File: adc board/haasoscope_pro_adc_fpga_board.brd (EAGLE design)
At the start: 224.5 x 160 mm, 569 parts, among them CN2 12Vin, IC1 ADC12DL2500ACF, IC10 TPS72325DBVR, IC13 LMH5401IRMST, IC14 LMH6401IRMZR, IC15 SN74AVC4T774PWR, IC17 DAC8562SDGSR, IC18 TLV9102IPWR, IC2 SN74AVC4T774PWR, IC21 LMH5401IRMST, IC22 TPS7A7200RGTR, IC23 TPS7A7200RGTR, IC24 TPS7A7200RGTR, IC25 TPS72325DBVR, IC26 TPS7A7200RGTR, IC27 TPS7A7200RGTR, IC28 TPS7A7200RGTR, IC29 LMH6401IRMZR, IC3 ADC122S021CIMM_NOPB, IC30 SN74AVC4T774PWR, IC33 TLV9102IPWR, IC4 TLV9102IPWR, IC5 EP4CE30F23C6N, IC6 EPCQ16ASI8N, IC7 TPS7A7200RGTR, IC8 FT232HQ, IC9 93LC56B, J1 2p-2.54, J10 8pin, J11 8pin, J13 8pin, J14 2x5, J15 test1, J2 test1, J3 2p-2.54, J30 2p-2.54, J31 2p-2.54, J32 2p-2.54, J33 2p-2.54, J34 2p-2.54, J35 2p-2.54, J36 2p-2.54, J37 2p-2.54, J39 2p-2.54, J4 2p-2.54, J40 2p-2.54, J41 2p-2.54, J42 2p-2.54, J43 2p-2.54, J44 2p-2.54, J45 2p-2.54, J46 2p-2.54, J8 8pin, K1 G6K-2F-RF-T-TR03_DC5, K2 G6K-2F-RF-T-TR03_DC5, K3 G6K-2F-RF-T-TR03_DC5, K4 G6K-2F-RF-T-TR03_DC5, K5 G6K-2F-RF-T-TR03_DC5, K6 TLP3475R_TP,F, K7 TLP3475R_TP,F, Q1 S8050, Q4 S8050, Q5 S8050, Q7 S8050, Q8 S8050, Q9 S8050, SW3 SKQGADE010, SW4 SKQGADE010, U2 ADF4350BCPZ, X1 USBC, Y2 OSCILLATORSMD-5X3, Y3 12MHz

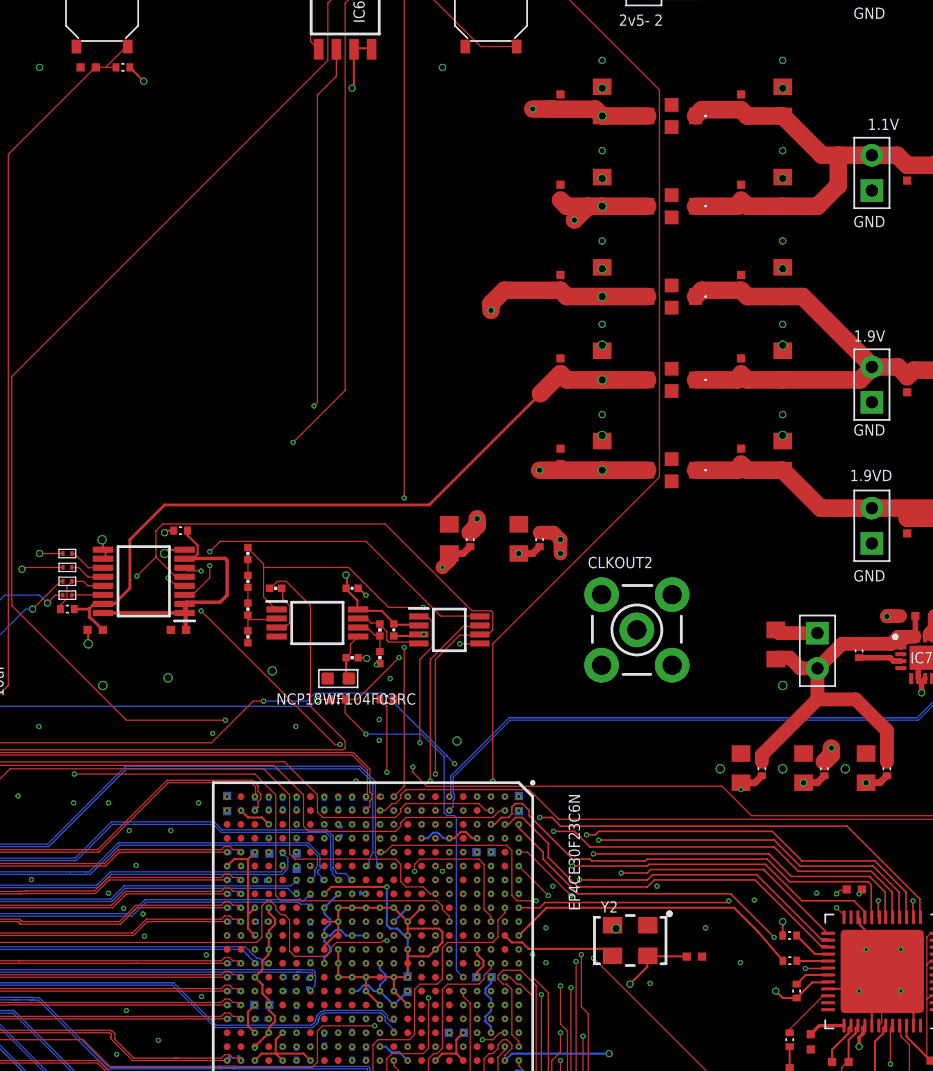
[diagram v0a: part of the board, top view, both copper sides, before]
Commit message: use 0.35mm vias instead of a few 0.5mm ones
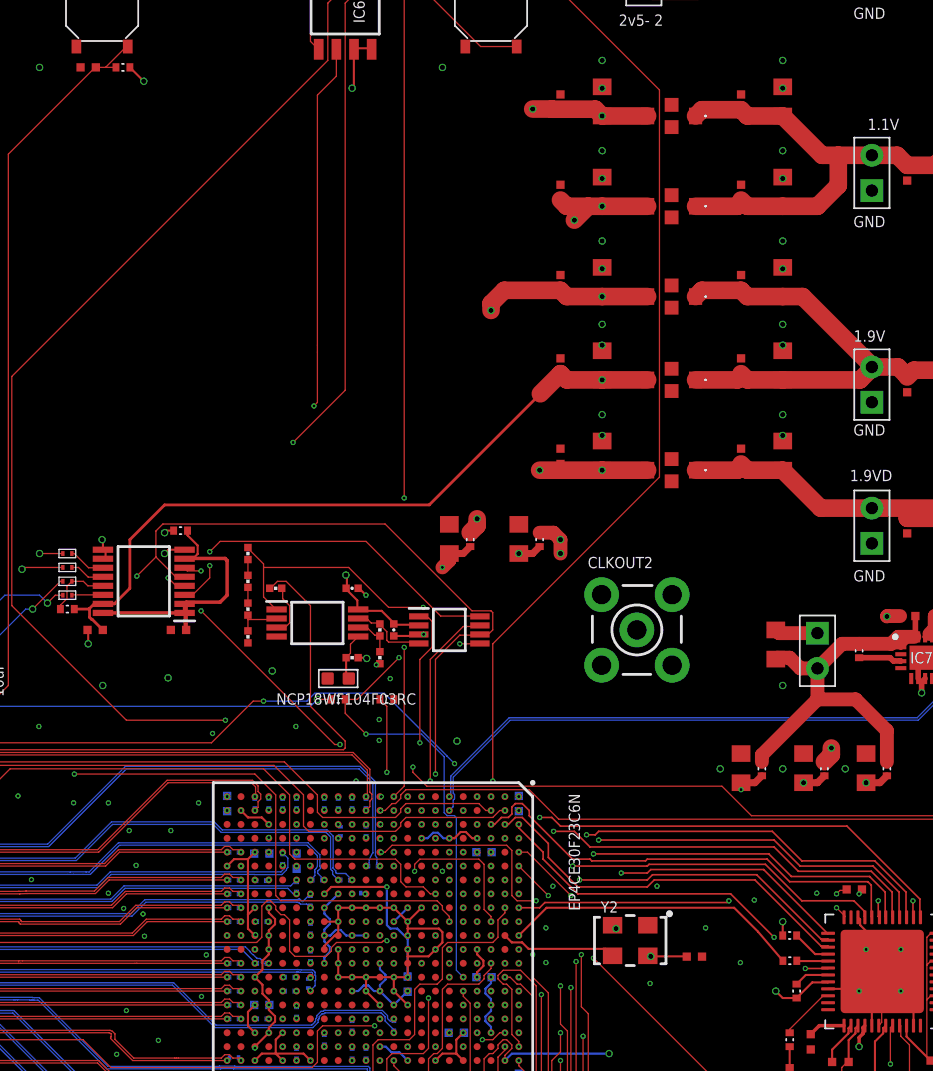
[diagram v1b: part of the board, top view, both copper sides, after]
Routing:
- net 3V3: track 157.8 -> 155.5 mm
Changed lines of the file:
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@@
 <wire x1="101.5" y1="68.65" x2="101.5" y2="69" width="0.1524" layer="16"/>
 <via x="103.5" y="82" extent="1-16" drill="0.2"/>
-<via x="129.5" y="80.5" extent="1-16" drill="0.5"/>
+<via x="129.5" y="80.5" extent="1-16" drill="0.35"/>
 <via x="69.5" y="68.5" extent="1-16" drill="0.2"/>
 <via x="73" y="69" extent="1-16" drill="0.2"/>
@@
 <via x="61.5" y="81" extent="1-16" drill="0.2"/>
 <via x="62" y="78" extent="1-16" drill="0.2"/>
-<via x="128.5" y="134.5" extent="1-16" drill="0.5"/>
-<via x="141.5" y="134.5" extent="1-16" drill="0.5"/>
-<via x="141.5" y="141" extent="1-16" drill="0.5"/>
-<via x="141.5" y="128" extent="1-16" drill="0.5"/>
-<via x="128.5" y="128" extent="1-16" drill="0.5"/>
-<via x="128.5" y="141" extent="1-16" drill="0.5"/>
-<via x="128.5" y="122.5" extent="1-16" drill="0.5"/>
-<via x="141.5" y="122.5" extent="1-16" drill="0.5"/>
-<via x="141.5" y="116" extent="1-16" drill="0.5"/>
-<via x="128.5" y="116" extent="1-16" drill="0.5"/>
-<via x="91.5" y="101" extent="1-16" drill="0.5"/>
+<via x="128.5" y="134.5" extent="1-16" drill="0.35"/>
+<via x="141.5" y="134.5" extent="1-16" drill="0.35"/>
+<via x="141.5" y="141" extent="1-16" drill="0.35"/>
+<via x="141.5" y="128" extent="1-16" drill="0.35"/>
+<via x="128.5" y="128" extent="1-16" drill="0.35"/>
+<via x="128.5" y="141" extent="1-16" drill="0.35"/>
+<via x="128.5" y="122.5" extent="1-16" drill="0.35"/>
+<via x="141.5" y="122.5" extent="1-16" drill="0.35"/>
+<via x="141.5" y="116" extent="1-16" drill="0.35"/>
+<via x="128.5" y="116" extent="1-16" drill="0.35"/>
+<via x="91.5" y="101" extent="1-16" drill="0.35"/>
 <via x="103.5" y="79" extent="1-16" drill="0.2"/>
 <via x="116.5" y="71" extent="1-16" drill="0.2"/>
@@
 <via x="53" y="94" extent="1-16" drill="0.35"/>
 <via x="68" y="97.5" extent="1-16" drill="0.35"/>
-<via x="92.55" y="98" extent="1-16" drill="0.5"/>
-<via x="104.75" y="99.05" extent="1-16" drill="0.5"/>
-<via x="118.05" y="94" extent="1-16" drill="0.5"/>
+<via x="92.55" y="98" extent="1-16" drill="0.35"/>
+<via x="104.75" y="99.05" extent="1-16" drill="0.35"/>
+<via x="118.05" y="94" extent="1-16" drill="0.35"/>
 <via x="72.55" y="94" extent="1-16" drill="0.2"/>
 <via x="69" y="90.5" extent="1-16" drill="0.2"/>
@@
 <via x="81.5" y="87" extent="1-16" drill="0.2"/>
 <via x="82.5" y="87" extent="1-16" drill="0.2"/>
-<via x="141.5" y="98" extent="1-16" drill="0.5"/>
+<via x="141.5" y="98" extent="1-16" drill="0.35"/>
 <wire x1="161.7" y1="101.2" x2="162.8521" y2="101.2" width="0.25" layer="1"/>
 <wire x1="162.8521" y1="101.2" x2="162.921" y2="101.1311" width="0.25" layer="1"/>
@@
 <via x="58.5" y="89" extent="1-16" drill="0.35"/>
 <via x="58.5" y="93" extent="1-16" drill="0.35"/>
-<via x="97" y="107.5" extent="1-16" drill="0.5"/>
+<via x="97" y="107.5" extent="1-16" drill="0.35"/>
 <wire x1="97" y1="107.5" x2="97.275" y2="107.775" width="0.1524" layer="1"/>
 <wire x1="97.275" y1="107.775" x2="98.438" y2="107.775" width="0.1524" layer="1"/>
-<via x="92.5" y="108.5" extent="1-16" drill="0.5"/>
+<via x="92.5" y="108.5" extent="1-16" drill="0.35"/>
 <wire x1="92.5" y1="108.5" x2="92.562" y2="108.438" width="0.1524" layer="1"/>
 <wire x1="92.562" y1="108.438" x2="92.562" y2="107.775" width="0.1524" layer="1"/>
@@
 <via x="141.5" y="136.5" extent="1-16" drill="0.35"/>
 <via x="141.5" y="143" extent="1-16" drill="0.35"/>
-<via x="137" y="92" extent="1-16" drill="0.5"/>
-<via x="141.5" y="92" extent="1-16" drill="0.5"/>
-<via x="146" y="92" extent="1-16" drill="0.5"/>
+<via x="137" y="92" extent="1-16" drill="0.35"/>
+<via x="141.5" y="92" extent="1-16" drill="0.35"/>
+<via x="146" y="92" extent="1-16" drill="0.35"/>
 <via x="152.930728125" y="35.729346875" extent="1-16" drill="0.2"/>
 <via x="178" y="35.712028125" extent="1-16" drill="0.2"/>
@@
 <contactref element="J1" pad="2"/>
 <contactref element="R207" pad="1"/>
-<via x="97.25" y="98.55" extent="1-16" drill="0.5"/>
+<via x="97.25" y="98.55" extent="1-16" drill="0.35"/>
 <contactref element="Q1" pad="2"/>
 <contactref element="R137" pad="P$1"/>
@@
 <via x="88.5" y="55" extent="1-16" drill="0.35"/>
 <via x="111.5" y="58.5" extent="1-16" drill="0.35"/>
-<via x="130.5" y="76.5" extent="1-16" drill="0.35"/>
+<via x="132" y="78.5" extent="1-16" drill="0.35"/>
 <via x="141" y="76" extent="1-16" drill="0.35"/>
 <via x="109.5" y="153.5" extent="1-16" drill="0.35"/>
@@
 <wire x1="110.5" y1="141" x2="110.625" y2="141.125" width="0.1524" layer="1"/>
 <wire x1="110.625" y1="143.75" x2="110.635" y2="143.8" width="0.1524" layer="1"/>
-<wire x1="131.75" y1="77.75" x2="131.75" y2="78.5" width="0.1524" layer="1"/>
-<wire x1="130.5" y1="76.5" x2="131.75" y2="77.75" width="0.1524" layer="1"/>
+<wire x1="132" y1="78.5" x2="131.75" y2="78.5" width="0.1524" layer="1"/>
 <wire x1="131.75" y1="78.5" x2="131.79" y2="78.54" width="0.1524" layer="1"/>
 <wire x1="52" y1="103.125" x2="55.375" y2="99.75" width="0.1524" layer="1"/>
@@
 <via x="69.5" y="81" extent="1-16" drill="0.2"/>
 <via x="72.5" y="81" extent="1-16" drill="0.2"/>
-<via x="128.5" y="126" extent="1-16" drill="0.5"/>
+<via x="128.5" y="126" extent="1-16" drill="0.35"/>
 <wire x1="72.5" y1="79" x2="72.45" y2="79" width="0.1524" layer="16"/>
 <wire x1="72.5" y1="80" x2="72.45" y2="80.1" width="0.1524" layer="16"/>
@@
 <via x="70.5" y="83" extent="1-16" drill="0.2"/>
 <via x="72.5" y="82" extent="1-16" drill="0.2"/>
-<via x="128.5" y="139" extent="1-16" drill="0.5"/>
+<via x="128.5" y="139" extent="1-16" drill="0.35"/>
 <wire x1="69.5" y1="82" x2="69.55" y2="82" width="0.1524" layer="16"/>
 <wire x1="69.5" y1="77" x2="69.55" y2="77" width="0.1524" layer="16"/>
@@
 <via x="74.5" y="78" extent="1-16" drill="0.2"/>
 <via x="74.5" y="83" extent="1-16" drill="0.2"/>
-<via x="128.5" y="132.5" extent="1-16" drill="0.5"/>
+<via x="128.5" y="132.5" extent="1-16" drill="0.35"/>
 <wire x1="74.5" y1="77" x2="74.55" y2="77.05" width="0.1524" layer="16"/>
 <wire x1="74.5" y1="81" x2="74.5" y2="80.5702125" width="0.1524" layer="16"/>
@@
 <wire x1="79.45" y1="78.9" x2="79.45" y2="78.95" width="0.1524" layer="16"/>
 <wire x1="79.45" y1="78.95" x2="79.5" y2="79" width="0.1524" layer="16"/>
-<via x="128.5" y="113.5" extent="1-16" drill="0.5"/>
+<via x="128.5" y="113.5" extent="1-16" drill="0.35"/>
 <wire x1="79.5" y1="80" x2="79.45" y2="80" width="0.1524" layer="16"/>
 <wire x1="128.5" y1="113.5" x2="125.5" y2="113.5" width="0.1524" layer="1"/>
@@
 <contactref element="C18" pad="2"/>
 <contactref element="C19" pad="2"/>
-<via x="128.5" y="120" extent="1-16" drill="0.5"/>
+<via x="128.5" y="120" extent="1-16" drill="0.35"/>
 <wire x1="125.5" y1="120.45" x2="124.05" y2="119" width="1.27" layer="1"/>
 <wire x1="124.05" y1="119" x2="116.05" y2="111" width="0.2032" layer="1"/>
@@
 <wire x1="106.5" y1="120.5" x2="115" y2="120.5" width="0.1524" layer="3"/>
 <wire x1="125" y1="110.5" x2="136.5" y2="110.5" width="0.1524" layer="3"/>
-<wire x1="136.5" y1="110.5" x2="136.5" y2="92.28234375" width="0.1524" layer="3"/>
-<wire x1="136.5" y1="92.28234375" x2="136.4468" y2="92.22914375" width="0.1524" layer="3"/>
-<wire x1="136.4468" y1="92.22914375" x2="136.4468" y2="91.77085625" width="0.1524" layer="3"/>
-<wire x1="136.4468" y1="91.77085625" x2="136.5" y2="91.71765625" width="0.1524" layer="3"/>
-<wire x1="136.5" y1="91.71765625" x2="136.5" y2="76.5" width="0.1524" layer="3"/>
+<wire x1="136.5" y1="110.5" x2="136.5" y2="76.5" width="0.1524" layer="3"/>
 <wire x1="136.5" y1="76.5" x2="131.5" y2="71.5" width="0.1524" layer="3"/>
 <wire x1="131.5" y1="71.5" x2="129" y2="71.5" width="0.1524" layer="3"/>

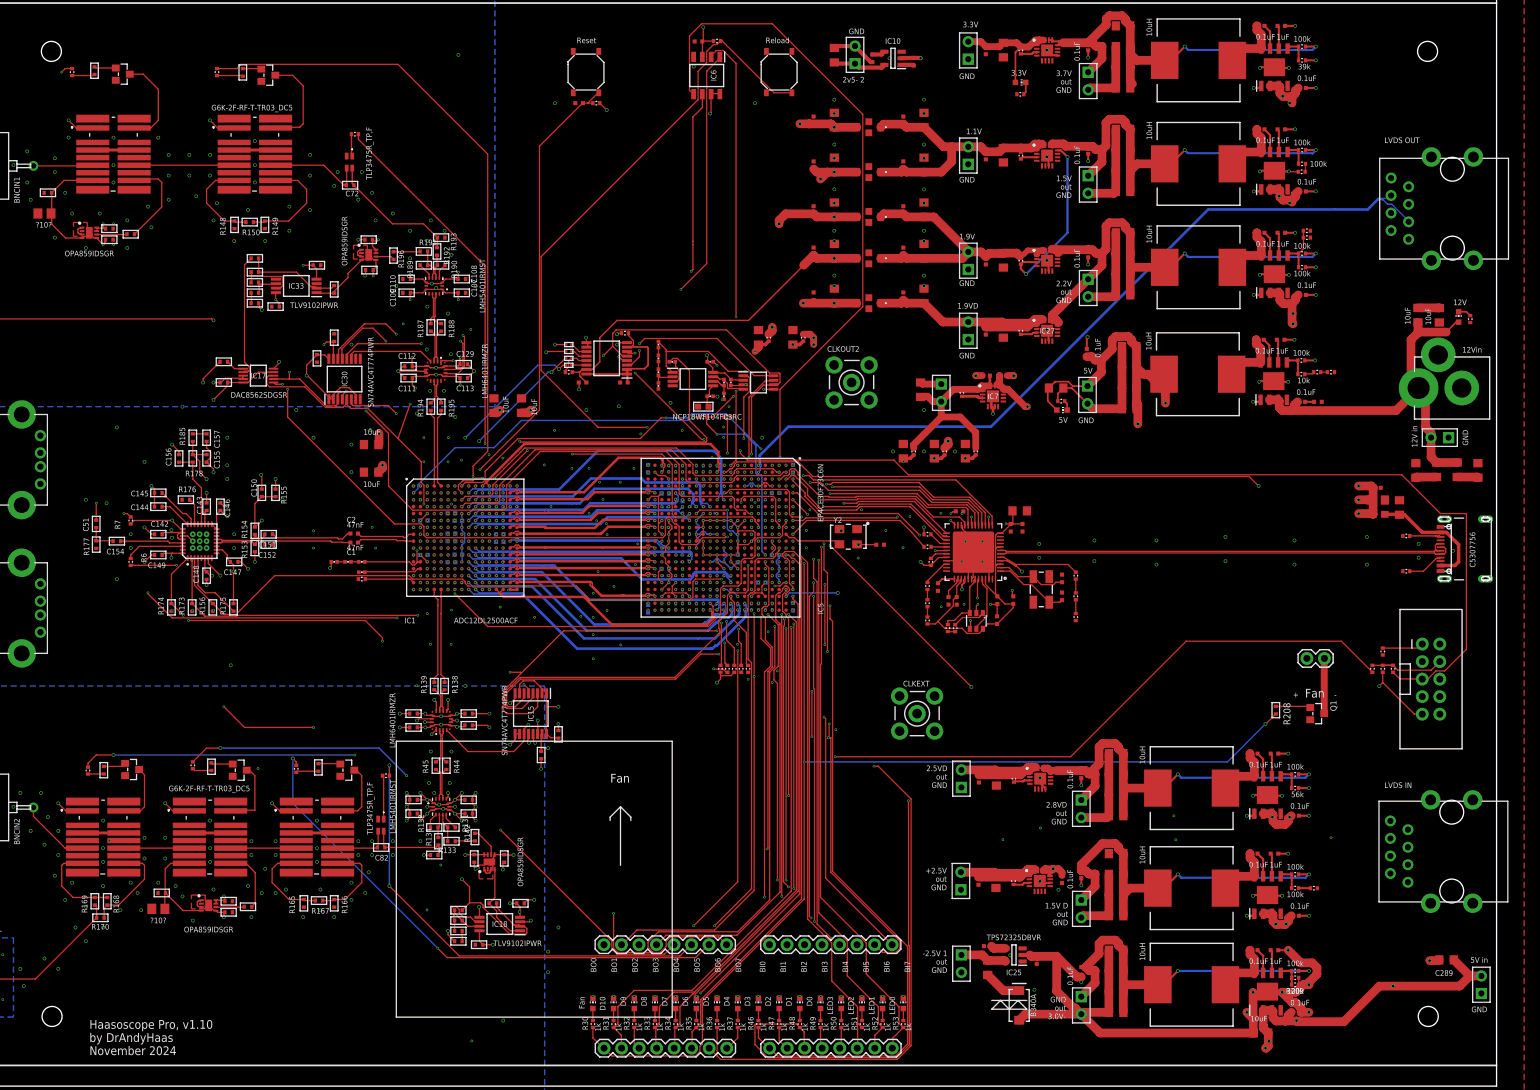
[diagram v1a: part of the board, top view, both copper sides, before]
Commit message: Add 1kHzOut50 SMA and ExtTrigIn SMA on back panel
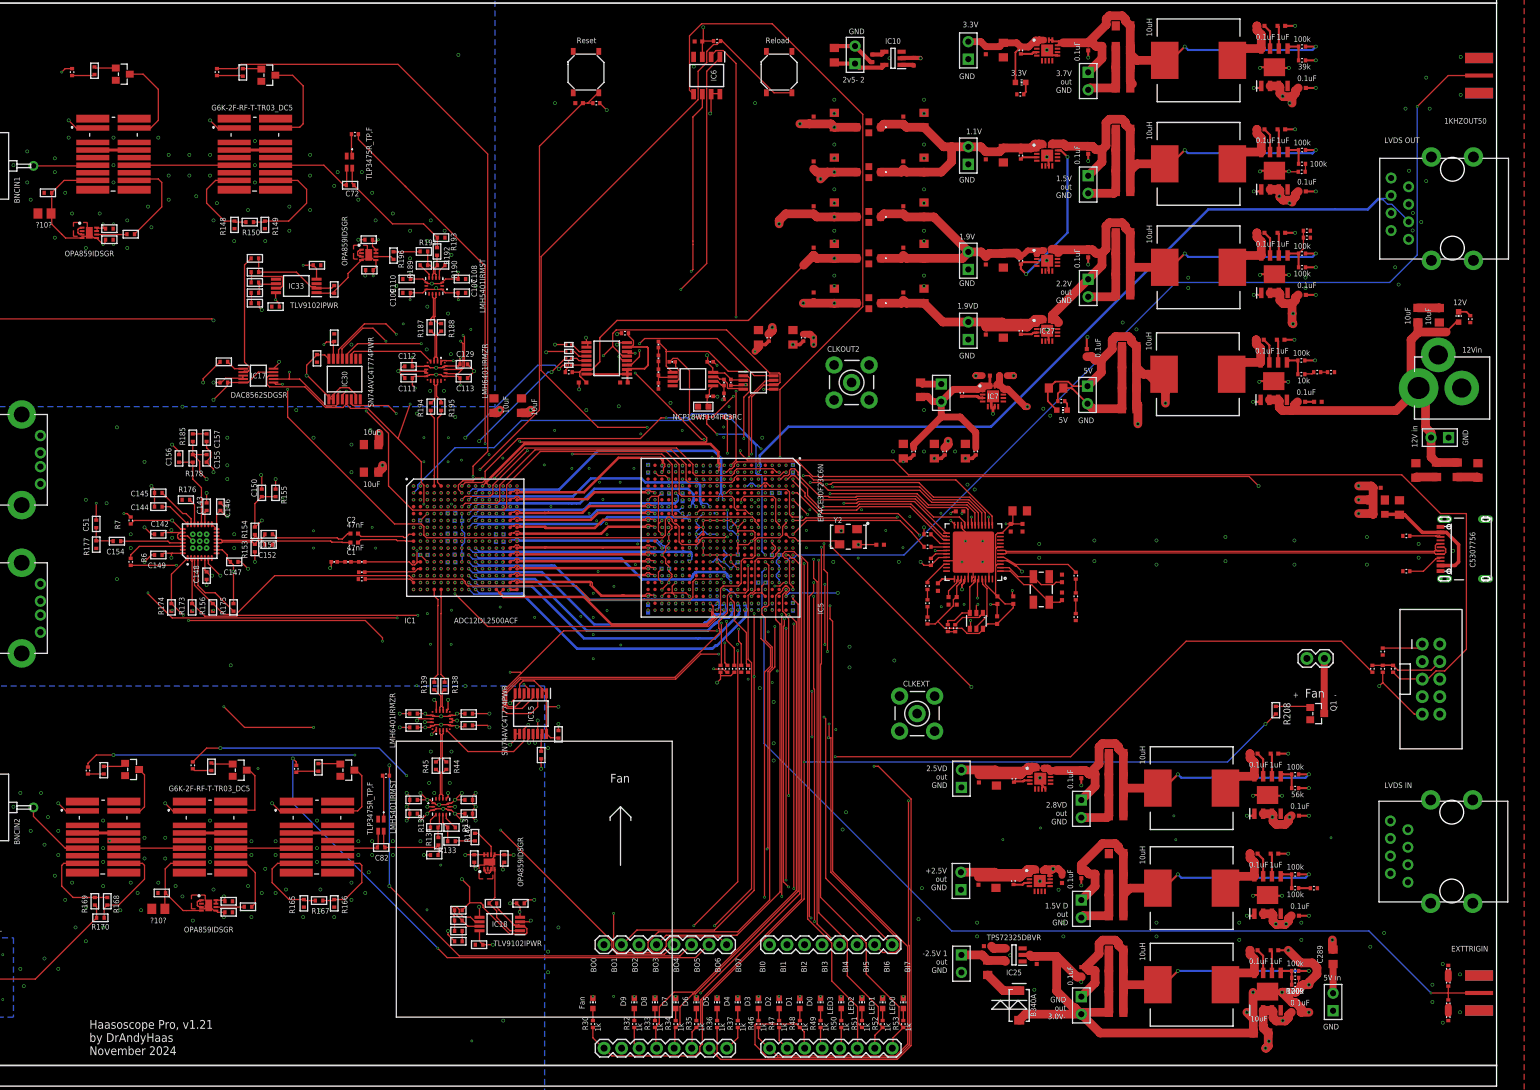
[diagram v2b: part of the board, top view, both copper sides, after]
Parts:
- removed LED31: red, adafruit:CHIP-LED0603
- added 1KHZOUT50, EXTTRIGIN: 50, adafruit:SMA_EDGELAUNCH
- added R136, R160, R210: 47, FlashPCB_Resistors:RES-0402
- R31: value 1k -> 47
- moved R31 121.0 mm to (217.5, 12.0)
- moved J46 21.6 mm to (200.8, 12.2)
- moved C289 16.4 mm to (200.8, 18.8), turned to 90 degrees
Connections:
- removed net BOARDIN4: IC5.E16, J8.5
- removed net DEBUGOUT10: IC5.B15, J11.7, R31.P$1
- new net 1KHZOUT50: 1KHZOUT50.P, IC5.B15
- new net EXTTRIGIN: EXTTRIGIN.P, IC5.E16, R160.P$2, R31.P$2
- new net N$13: R136.P$2, R31.P$1
- net GND: now also 1KHZOUT50.GND@1, 1KHZOUT50.GND@2, 1KHZOUT50.GND@3, 1KHZOUT50.GND@4, EXTTRIGIN.GND@1, EXTTRIGIN.GND@2, EXTTRIGIN.GND@3, EXTTRIGIN.GND@4, J11.7, J8.5, R136.P$1, R210.P$1; no longer LED31.C
- net N$31: now also R160.P$1, R210.P$2; no longer LED31.A, R31.P$2
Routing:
- net EXTTRIGIN: track 0.00 -> 146.3 mm, vias 0 -> 2
- net 1KHZOUT50: track 0.00 -> 142.3 mm, vias 0 -> 2
- net DEBUGOUT10: track 86.9 -> 0.00 mm, vias 2 -> 0
- net BOARDIN4: track 59.5 -> 0.00 mm, vias 3 -> 0
- net 5V: track 162.3 -> 132.0 mm, vias 26 -> 25
- net N$13: track 0.00 -> 1.00 mm
- net N$31: track 1.75 -> 1.00 mm
- net GND: vias 561 -> 614
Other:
- board text added: "Haasoscope Pro, v1.21 by DrAndyHaas November 2024"
- board text removed: "D10"
- board text removed: "Haasoscope Pro, v1.10 by DrAndyHaas November 2024"
